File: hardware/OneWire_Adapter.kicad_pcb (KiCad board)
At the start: 2 copper layers, 40 x 35 mm, 11 parts, among them T1 BC547, T2 BC547, X1 USART, X2 1-Wire

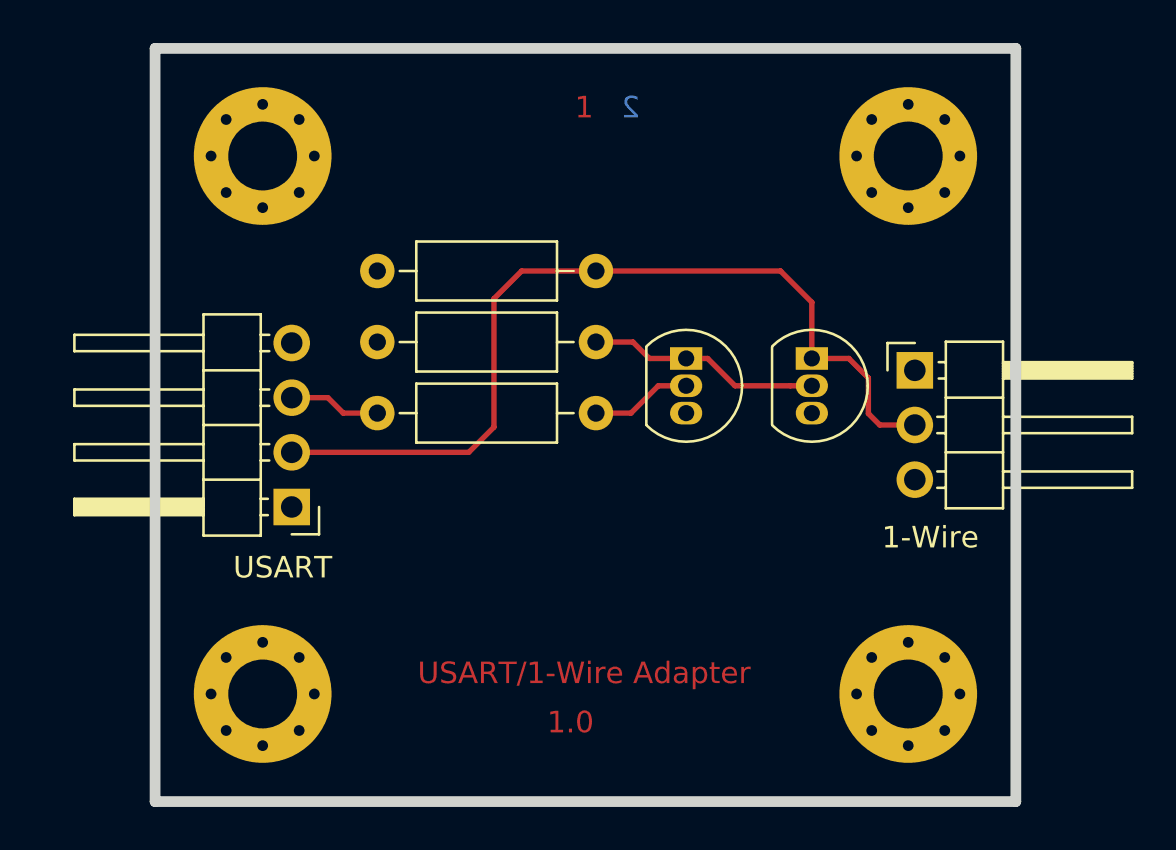
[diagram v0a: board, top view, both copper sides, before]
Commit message: Add level shifter
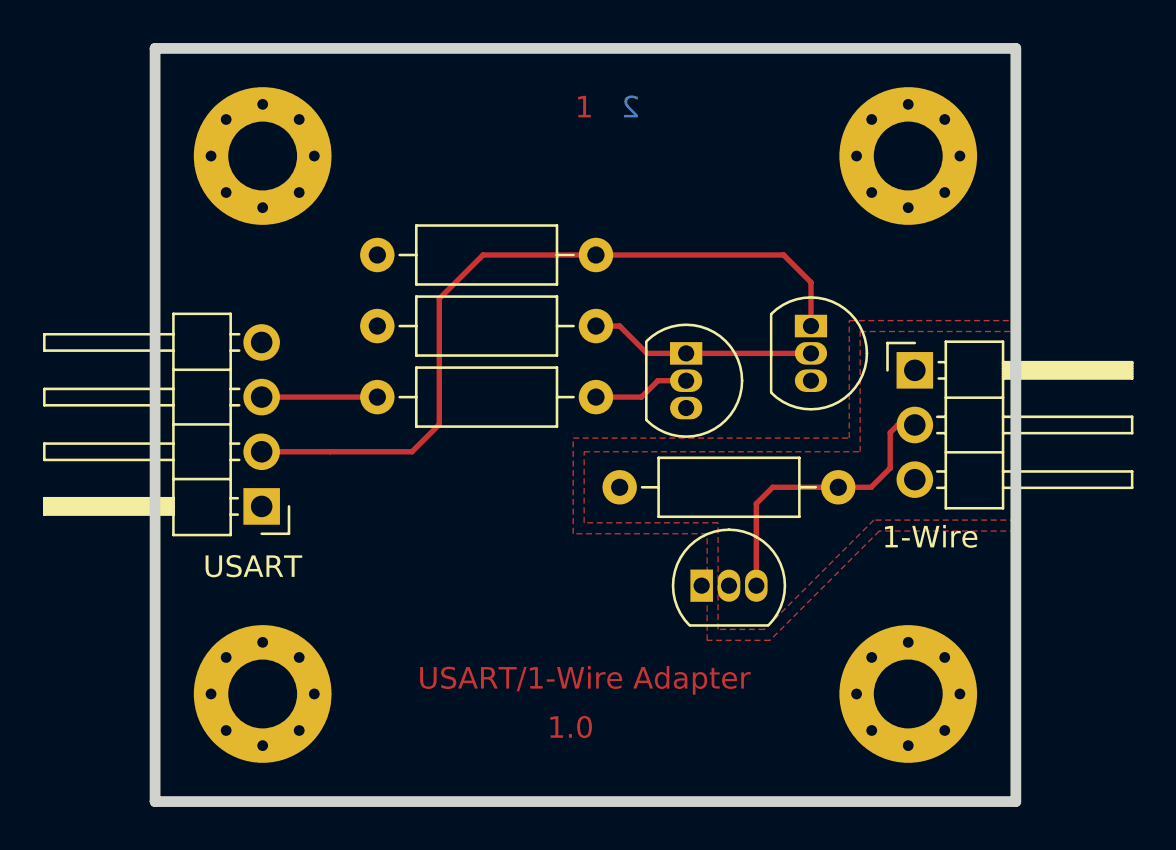
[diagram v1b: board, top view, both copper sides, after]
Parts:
- added R4: 10k, Resistor_THT:R_Axial_DIN0207_L6.3mm_D2.5mm_P10.16mm_Horizontal, F.Cu at (143.0, 102.8)
- added T3: BS170, Package_TO_SOT_THT:TO-92_Inline, F.Cu at (146.8, 107.3)
- moved T2 1.51 mm to (151.9, 95.3)
- moved X1 1.40 mm to (126.3, 103.7)
- moved R1 0.74 mm to (131.7, 98.6)
- moved R2 0.74 mm to (131.7, 95.3)
- moved R3 0.74 mm to (131.7, 92.0)
- moved T1 0.24 mm to (146.1, 96.5)
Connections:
- R3 pad 2: /1-Wire -> /RxD
- T2 pad 1: /1-Wire -> /RxD
- X1 pad 2: /1-Wire -> /RxD
- X2 pad 1: /Vcc -> /Vcc2
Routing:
- net /RxD: track 0.00 -> 35.3 mm
- net /1-Wire: track 41.4 -> 13.7 mm
- net /TxD: track 4.28 -> 5.38 mm
- added copper zone on F.Cu, net /Vcc2

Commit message: Add new schematics
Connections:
- net /Vcc2 renamed /VL
- R2 pad 1: /Vcc -> /VH
- R3 pad 1: /Vcc -> /VH
- T3 pad 1: /Vcc -> /RxD
- X1 pad 4: /Vcc -> /VH
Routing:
- net /RxD: track 35.3 -> 51.1 mm, vias 0 -> 1
- added copper zone on F.Cu, net /VH
- removed copper zone on F.Cu, net /Vcc
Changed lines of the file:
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@@
     (thickness 1.6)
     (drawings 14)
-    (tracks 25)
+    (tracks 30)
     (zones 0)
     (modules 13)
@@
   (net 2 /TxD)
   (net 3 "Net-(R2-Pad2)")
-  (net 4 /Vcc)
-  (net 5 /1-Wire)
-  (net 6 /GND)
-  (net 7 /RxD)
-  (net 8 /Vcc2)
+  (net 4 /1-Wire)
+  (net 5 /GND)
+  (net 6 /RxD)
+  (net 7 /VH)
+  (net 8 /VL)
   (net_class Default "Dies ist die voreingestellte Netzklasse."
     (clearance 0.2)
@@
     (add_net /RxD)
     (add_net /TxD)
-    (add_net /Vcc)
-    (add_net /Vcc2)
+    (add_net /VH)
+    (add_net /VL)
     (add_net "Net-(R1-Pad2)")
     (add_net "Net-(R2-Pad2)")
@@
     )
     (pad 1 thru_hole rect (at 0 0) (size 1.05 1.5) (drill 0.75) (layers *.Cu *.Mask)
-      (net 4 /Vcc))
+      (net 6 /RxD))
     (pad 3 thru_hole oval (at 2.54 0) (size 1.05 1.5) (drill 0.75) (layers *.Cu *.Mask)
-      (net 5 /1-Wire))
+      (net 4 /1-Wire))
     (pad 2 thru_hole oval (at 1.27 0) (size 1.05 1.5) (drill 0.75) (layers *.Cu *.Mask)
-      (net 8 /Vcc2))
+      (net 8 /VL))
     (model ${KISYS3DMOD}/Package_TO_SOT_THT.3dshapes/TO-92_Inline.wrl
       (at (xyz 0 0 0))
@@
     (fp_line (start 1.93 -1.25) (end 1.93 1.25) (layer F.Fab) (width 0.1))
     (pad 2 thru_hole oval (at 10.16 0) (size 1.6 1.6) (drill 0.8) (layers *.Cu *.Mask)
-      (net 5 /1-Wire))
+      (net 4 /1-Wire))
     (pad 1 thru_hole circle (at 0 0) (size 1.6 1.6) (drill 0.8) (layers *.Cu *.Mask)
-      (net 8 /Vcc2))
+      (net 8 /VL))
     (model ${KISYS3DMOD}/Resistor_THT.3dshapes/R_Axial_DIN0207_L6.3mm_D2.5mm_P10.16mm_Horizontal.wrl
       (at (xyz 0 0 0))
@@
     (fp_line (start 2.135 -1.27) (end 4.04 -1.27) (layer F.Fab) (width 0.1))
     (pad 3 thru_hole oval (at 0 5.08) (size 1.7 1.7) (drill 1) (layers *.Cu *.Mask)
-      (net 6 /GND))
+      (net 5 /GND))
     (pad 2 thru_hole oval (at 0 2.54) (size 1.7 1.7) (drill 1) (layers *.Cu *.Mask)
-      (net 5 /1-Wire))
+      (net 4 /1-Wire))
     (pad 1 thru_hole rect (at 0 0) (size 1.7 1.7) (drill 1) (layers *.Cu *.Mask)
-      (net 8 /Vcc2))
+      (net 8 /VL))
     (model ${KISYS3DMOD}/Connector_PinHeader_2.54mm.3dshapes/PinHeader_1x03_P2.54mm_Horizontal.wrl
       (at (xyz 0 0 0))
@@
     (fp_line (start 2.135 -1.27) (end 4.04 -1.27) (layer F.Fab) (width 0.1))
     (pad 4 thru_hole oval (at 0 7.62 180) (size 1.7 1.7) (drill 1) (layers *.Cu *.Mask)
-      (net 4 /Vcc))
+      (net 7 /VH))
     (pad 3 thru_hole oval (at 0 5.08 180) (size 1.7 1.7) (drill 1) (layers *.Cu *.Mask)
       (net 2 /TxD))
     (pad 2 thru_hole oval (at 0 2.54 180) (size 1.7 1.7) (drill 1) (layers *.Cu *.Mask)
-      (net 7 /RxD))
+      (net 6 /RxD))
     (pad 1 thru_hole rect (at 0 0 180) (size 1.7 1.7) (drill 1) (layers *.Cu *.Mask)
-      (net 6 /GND))
+      (net 5 /GND))
     (model ${KISYS3DMOD}/Connector_PinHeader_2.54mm.3dshapes/PinHeader_1x04_P2.54mm_Horizontal.wrl
       (at (xyz 0 0 0))
@@
     )
     (pad 1 thru_hole rect (at 0 0 270) (size 1.05 1.5) (drill 0.75) (layers *.Cu *.Mask)
-      (net 7 /RxD))
+      (net 6 /RxD))
     (pad 3 thru_hole oval (at 2.54 0 270) (size 1.05 1.5) (drill 0.75) (layers *.Cu *.Mask)
-      (net 6 /GND))
+      (net 5 /GND))
     (pad 2 thru_hole oval (at 1.27 0 270) (size 1.05 1.5) (drill 0.75) (layers *.Cu *.Mask)
       (net 3 "Net-(R2-Pad2)"))
@@
       (net 3 "Net-(R2-Pad2)"))
     (pad 3 thru_hole oval (at 2.54 0 270) (size 1.05 1.5) (drill 0.75) (layers *.Cu *.Mask)
-      (net 6 /GND))
+      (net 5 /GND))
     (pad 2 thru_hole oval (at 1.27 0 270) (size 1.05 1.5) (drill 0.75) (layers *.Cu *.Mask)
       (net 1 "Net-(R1-Pad2)"))
@@
     (fp_line (start 1.93 -1.25) (end 1.93 1.25) (layer F.Fab) (width 0.1))
     (pad 2 thru_hole oval (at 10.16 0) (size 1.6 1.6) (drill 0.8) (layers *.Cu *.Mask)
-      (net 7 /RxD))
+      (net 6 /RxD))
     (pad 1 thru_hole circle (at 0 0) (size 1.6 1.6) (drill 0.8) (layers *.Cu *.Mask)
-      (net 4 /Vcc))
+      (net 7 /VH))
     (model ${KISYS3DMOD}/Resistor_THT.3dshapes/R_Axial_DIN0207_L6.3mm_D2.5mm_P10.16mm_Horizontal.wrl
       (at (xyz 0 0 0))
@@
       (net 3 "Net-(R2-Pad2)"))
     (pad 1 thru_hole circle (at 0 0) (size 1.6 1.6) (drill 0.8) (layers *.Cu *.Mask)
-      (net 4 /Vcc))
+      (net 7 /VH))
     (model ${KISYS3DMOD}/Resistor_THT.3dshapes/R_Axial_DIN0207_L6.3mm_D2.5mm_P10.16mm_Horizontal.wrl
       (at (xyz 0 0 0))
@@
   (segment (start 141.859 95.268) (end 142.961 95.268) (width 0.25) (layer F.Cu) (net 3))
   (segment (start 142.961 95.268) (end 144.231 96.538) (width 0.25) (layer F.Cu) (net 3))
-  (segment (start 150.073 102.761) (end 153.121 102.761) (width 0.25) (layer F.Cu) (net 5))
-  (segment (start 149.311 107.333) (end 149.311 103.523) (width 0.25) (layer F.Cu) (net 5))
-  (segment (start 149.311 103.523) (end 150.073 102.761) (width 0.25) (layer F.Cu) (net 5))
-  (segment (start 155.889 99.866) (end 155.534 100.221) (width 0.25) (layer F.Cu) (net 5))
-  (segment (start 156.677 99.866) (end 155.889 99.866) (width 0.25) (layer F.Cu) (net 5))
-  (segment (start 155.534 100.221) (end 155.534 101.872) (width 0.25) (layer F.Cu) (net 5))
-  (segment (start 155.534 101.872) (end 154.645 102.761) (width 0.25) (layer F.Cu) (net 5))
-  (segment (start 154.645 102.761) (end 153.121 102.761) (width 0.25) (layer F.Cu) (net 5))
-  (segment (start 151.851 93.236) (end 151.851 95.268) (width 0.25) (layer F.Cu) (net 7))
-  (segment (start 141.859 91.966) (end 150.581 91.966) (width 0.25) (layer F.Cu) (net 7))
-  (segment (start 150.581 91.966) (end 151.851 93.236) (width 0.25) (layer F.Cu) (net 7))
-  (segment (start 129.499 101.11) (end 126.324 101.11) (width 0.25) (layer F.Cu) (net 7))
-  (segment (start 133.309 101.11) (end 129.499 101.11) (width 0.25) (layer F.Cu) (net 7))
-  (segment (start 134.579 99.84) (end 133.309 101.11) (width 0.25) (layer F.Cu) (net 7))
-  (segment (start 134.579 93.998) (end 134.579 99.84) (width 0.25) (layer F.Cu) (net 7))
-  (segment (start 141.859 91.966) (end 136.611 91.966) (width 0.25) (layer F.Cu) (net 7))
-  (segment (start 136.611 91.966) (end 134.579 93.998) (width 0.25) (layer F.Cu) (net 7))
-  (zone (net 6) (net_name /GND) (layer B.Cu) (hatch edge 0.508)
+  (segment (start 150.073 102.761) (end 153.121 102.761) (width 0.25) (layer F.Cu) (net 4))
+  (segment (start 149.311 107.333) (end 149.311 103.523) (width 0.25) (layer F.Cu) (net 4))
+  (segment (start 149.311 103.523) (end 150.073 102.761) (width 0.25) (layer F.Cu) (net 4))
+  (segment (start 155.889 99.866) (end 155.534 100.221) (width 0.25) (layer F.Cu) (net 4))
+  (segment (start 156.677 99.866) (end 155.889 99.866) (width 0.25) (layer F.Cu) (net 4))
+  (segment (start 155.534 100.221) (end 155.534 101.872) (width 0.25) (layer F.Cu) (net 4))
+  (segment (start 155.534 101.872) (end 154.645 102.761) (width 0.25) (layer F.Cu) (net 4))
+  (segment (start 154.645 102.761) (end 153.121 102.761) (width 0.25) (layer F.Cu) (net 4))
+  (segment (start 151.851 93.236) (end 151.851 95.268) (width 0.25) (layer F.Cu) (net 6))
+  (segment (start 141.859 91.966) (end 150.581 91.966) (width 0.25) (layer F.Cu) (net 6))
+  (segment (start 150.581 91.966) (end 151.851 93.236) (width 0.25) (layer F.Cu) (net 6))
+  (segment (start 129.499 101.11) (end 126.324 101.11) (width 0.25) (layer F.Cu) (net 6))
+  (segment (start 133.309 101.11) (end 129.499 101.11) (width 0.25) (layer F.Cu) (net 6))
+  (segment (start 134.579 99.84) (end 133.309 101.11) (width 0.25) (layer F.Cu) (net 6))
+  (segment (start 134.579 93.998) (end 134.579 99.84) (width 0.25) (layer F.Cu) (net 6))
+  (segment (start 141.859 91.966) (end 136.611 91.966) (width 0.25) (layer F.Cu) (net 6))
+  (segment (start 136.611 91.966) (end 134.579 93.998) (width 0.25) (layer F.Cu) (net 6))
+  (segment (start 151.851 95.268) (end 149.057 95.268) (width 0.25) (layer F.Cu) (net 6))
+  (via (at 149.057 95.268) (size 0.8) (drill 0.4) (layers F.Cu B.Cu) (net 6))
+  (segment (start 146.771 104.285) (end 146.771 107.333) (width 0.25) (layer B.Cu) (net 6))
+  (segment (start 149.057 95.268) (end 149.057 101.999) (width 0.25) (layer B.Cu) (net 6))
+  (segment (start 149.057 101.999) (end 146.771 104.285) (width 0.25) (layer B.Cu) (net 6))
+  (zone (net 5) (net_name /GND) (layer B.Cu) (hatch edge 0.508)
     (connect_pads (clearance 0.508))
     (min_thickness 0.254)
@@
     )
   )
-  (zone (net 8) (net_name /Vcc2) (layer F.Cu) (hatch edge 0.508)
+  (zone (net 8) (net_name /VL) (layer F.Cu) (hatch edge 0.508)
     (connect_pads (clearance 0.508))
     (min_thickness 0.254)
@@
     )
   )
-  (zone (net 4) (net_name /Vcc) (layer F.Cu) (hatch edge 0.508)
+  (zone (net 7) (net_name /VH) (layer F.Cu) (hatch edge 0.508)
     (connect_pads (clearance 0.508))
     (min_thickness 0.254)

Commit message: Update project directory
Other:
- board text added: "1-Wire / USART Adapter"
- board text added: "Bot"
- board text added: "Top"
- board text removed: "1"
- board text removed: "2"
- board text removed: "USART/1-Wire Adapter"
